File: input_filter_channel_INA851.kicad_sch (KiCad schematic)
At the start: 28 parts, among them K1 EE2-12TNU-L, U101 INA851

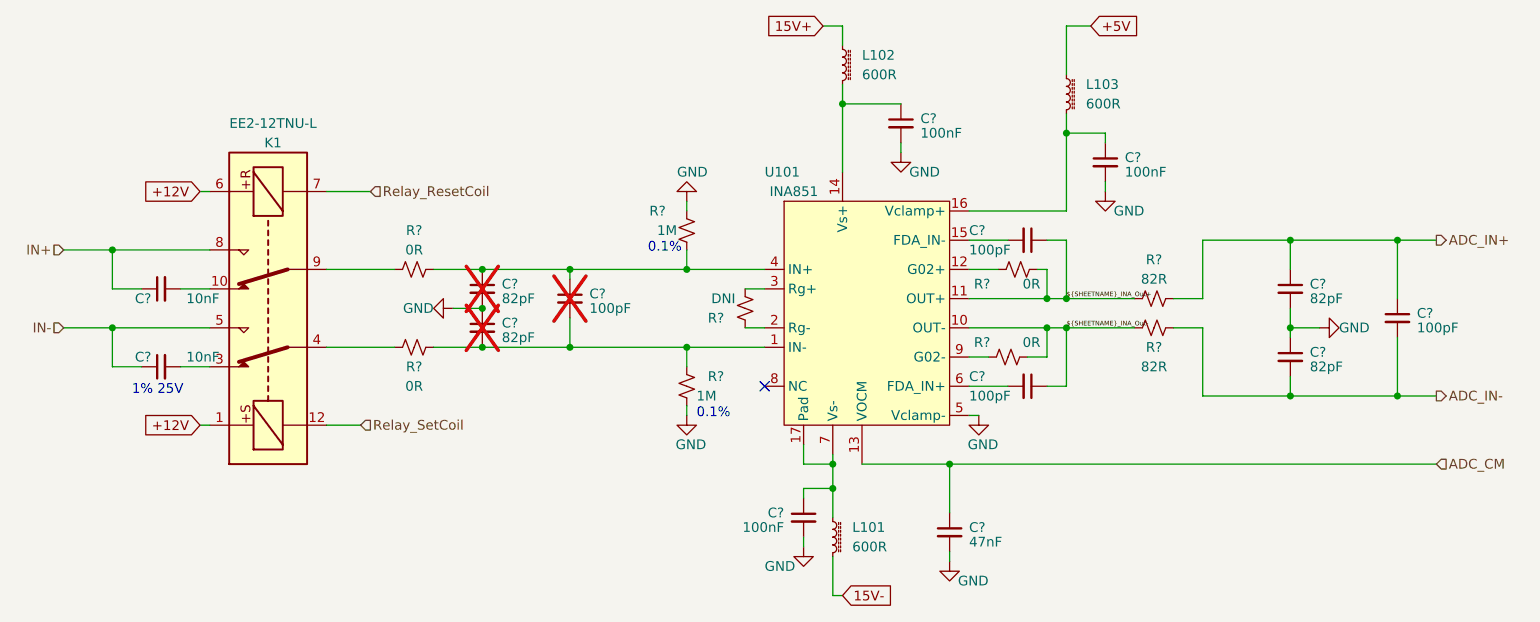
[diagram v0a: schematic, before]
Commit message: Updating design to cover reworks
Updating design to cover reworks.
This should now match what has been delivered to NASA GRE-ATF after the board reworks.
All outputs have been regenerated
Changes are:
1)Changed the clock splitter part to a 2.5V compatible part
2)Changed some caps on the MCLK lines to 0R resitors
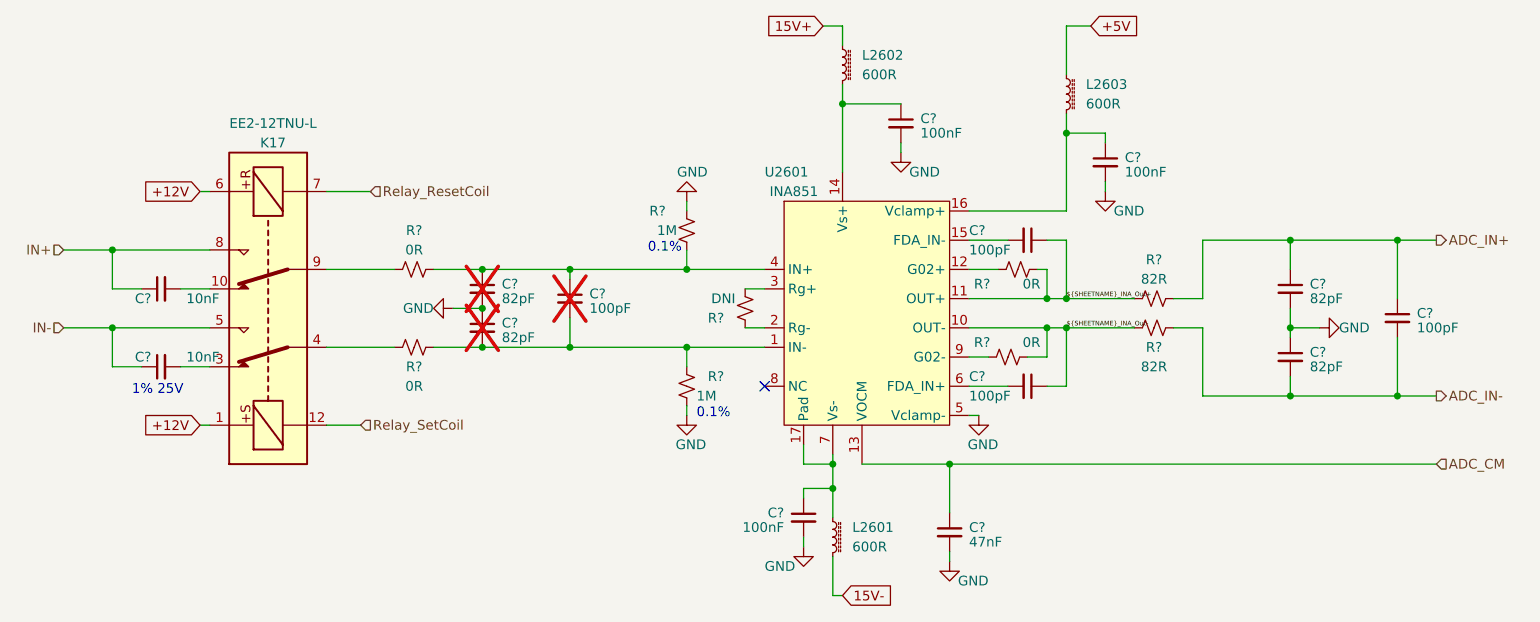
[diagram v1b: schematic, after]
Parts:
- R? (x4): footprint Resistor_SMD:R_0402_1005Metric -> Resistor_SMD:R_0603_1608Metric
- renumbered K1 to K17, L101 to L2601, L102 to L2602, L103 to L2603, U101 to U2601
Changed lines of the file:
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@@
 			)
 		)
-		(property "Footprint" "Resistor_SMD:R_0402_1005Metric"
+		(property "Footprint" "Resistor_SMD:R_0603_1608Metric"
 			(at 176.53 97.79 0)
 			(effects
@@
 			)
 		)
-		(property "Footprint" "Resistor_SMD:R_0402_1005Metric"
+		(property "Footprint" "Resistor_SMD:R_0603_1608Metric"
 			(at 177.8 86.36 0)
 			(effects
@@
 		(on_board yes)
 		(dnp no)
-		(property "Reference" "U101"
+		(property "Reference" "U2601"
 			(at 144.78 73.66 0)
 			(effects
@@
 		(dnp no)
 		(fields_autoplaced yes)
-		(property "Reference" "L101"
+		(property "Reference" "L2601"
 			(at 156.21 120.015 0)
 			(effects
@@
 		(dnp no)
 		(fields_autoplaced yes)
-		(property "Reference" "L103"
+		(property "Reference" "L2603"
 			(at 186.69 62.23 0)
 			(effects
@@
 			)
 		)
-		(property "Footprint" "Resistor_SMD:R_0402_1005Metric"
+		(property "Footprint" "Resistor_SMD:R_0603_1608Metric"
 			(at 99.06 86.36 0)
 			(effects
@@
 		(dnp no)
 		(fields_autoplaced yes)
-		(property "Reference" "L102"
+		(property "Reference" "L2602"
 			(at 157.48 58.42 0)
 			(effects
@@
 			)
 		)
-		(property "Footprint" "Resistor_SMD:R_0402_1005Metric"
+		(property "Footprint" "Resistor_SMD:R_0603_1608Metric"
 			(at 99.06 96.52 0)
 			(effects
@@
 		(on_board yes)
 		(dnp no)
-		(property "Reference" "K1"
+		(property "Reference" "K17"
 			(at 80.645 69.85 90)
 			(effects

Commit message: Opened & Saved Project in Kicad 9
- Opened & Saved Project in Kicad 9
- Added .gitignore from main
- Added sym-lib-table to link the unchanged symbol libs to the project
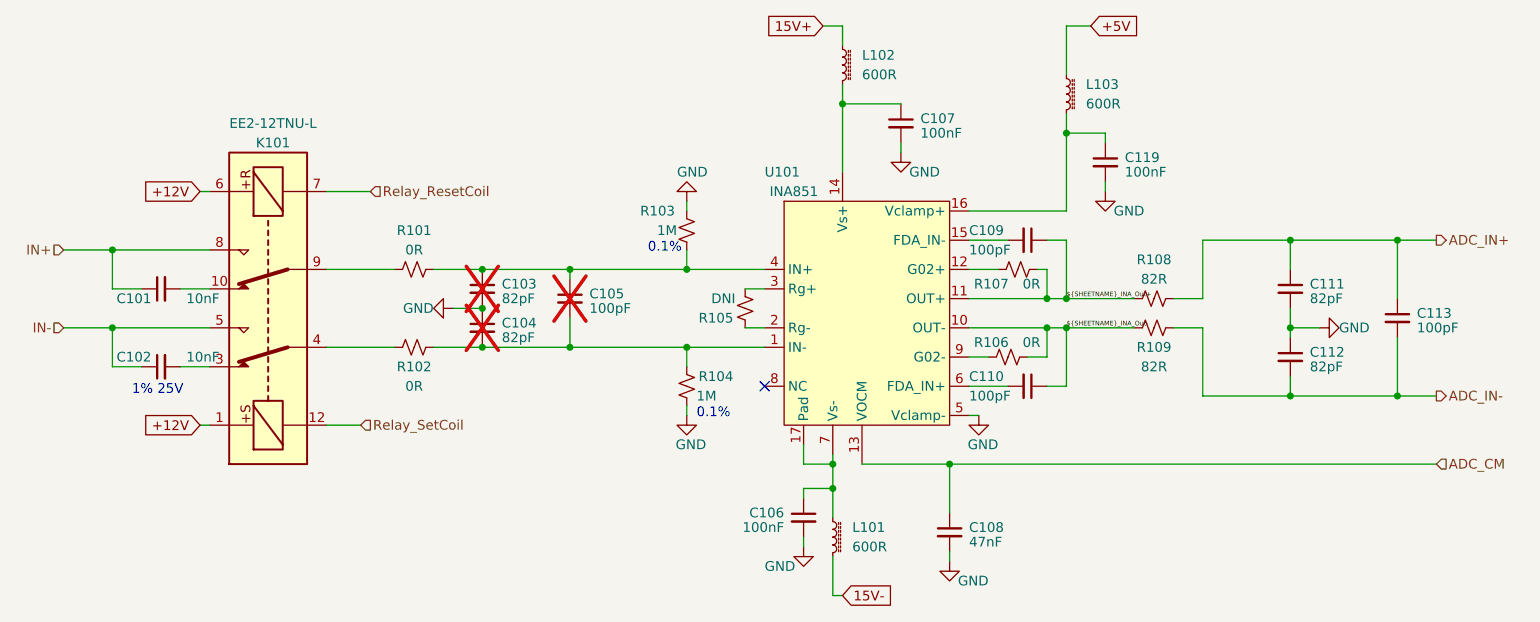
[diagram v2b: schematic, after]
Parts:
- gave numbers to parts that had none: 23
- renumbered K17 to K101, L2601 to L101, L2602 to L102, L2603 to L103, U2601 to U101
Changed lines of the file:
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@@
 (kicad_sch
-	(version 20231120)
+	(version 20250114)
 	(generator "eeschema")
-	(generator_version "8.0")
+	(generator_version "9.0")
 	(paper "A4")
 	(title_block
@@
 		(company "OspreyDCS")
 	)
+	(text "1% 25V\n"
+		(exclude_from_sim no)
+		(at 62.23 102.87 0)
+		(effects
+			(font
+				(size 1.27 1.27)
+			)
+			(justify left bottom)
+		)
+	)
+	(text "0.1%\n\n"
+		(exclude_from_sim no)
+		(at 129.54 86.36 0)
+		(effects
+			(font
+				(size 1.27 1.27)
+			)
+			(justify left bottom)
+		)
+	)
+	(text "0.1%\n\n"
+		(exclude_from_sim no)
+		(at 135.89 107.95 0)
+		(effects
+			(font
+				(size 1.27 1.27)
+			)
+			(justify left bottom)
+		)
+	)
 	(junction
 		(at 59.69 93.98)
@@
 		)
 	)
-	(text "1% 25V\n"
-		(exclude_from_sim no)
-		(at 62.23 102.87 0)
-		(effects
-			(font
-				(size 1.27 1.27)
-			)
-			(justify left bottom)
-		)
-	)
-	(text "0.1%\n\n"
-		(exclude_from_sim no)
-		(at 129.54 86.36 0)
-		(effects
-			(font
-				(size 1.27 1.27)
-			)
-			(justify left bottom)
-		)
-	)
-	(text "0.1%\n\n"
-		(exclude_from_sim no)
-		(at 135.89 107.95 0)
-		(effects
-			(font
-				(size 1.27 1.27)
-			)
-			(justify left bottom)
-		)
-	)
 	(label "${SHEETNAME}_INA_Out-"
 		(at 184.15 93.98 0)
-		(fields_autoplaced yes)
 		(effects
 			(font
@@
 	(label "${SHEETNAME}_INA_Out+"
 		(at 184.15 90.17 0)
-		(fields_autoplaced yes)
 		(effects
 			(font
@@
 		(shape input)
 		(at 93.345 76.2 0)
-		(fields_autoplaced yes)
 		(effects
 			(font
@@
 		(shape input)
 		(at 92.075 106.68 0)
-		(fields_autoplaced yes)
 		(effects
 			(font
@@
 		(shape input)
 		(at 53.34 93.98 180)
-		(fields_autoplaced yes)
 		(effects
 			(font
@@
 		(shape output)
 		(at 232.41 102.87 0)
-		(fields_autoplaced yes)
 		(effects
 			(font
@@
 		(shape input)
 		(at 232.41 111.76 0)
-		(fields_autoplaced yes)
 		(effects
 			(font
@@
 		(shape input)
 		(at 53.34 83.82 180)
-		(fields_autoplaced yes)
 		(effects
 			(font
@@
 		(shape output)
 		(at 232.41 82.55 0)
-		(fields_autoplaced yes)
 		(effects
 			(font
@@
 		(on_board yes)
 		(dnp no)
-		(property "Reference" "C?"
+		(property "Reference" "C102"
 			(at 64.77 97.79 90)
 			(effects
@@
 		(on_board yes)
 		(dnp no)
-		(property "Reference" "#PWR?"
+		(property "Reference" "#PWR0107"
 			(at 162.56 77.47 0)
 			(effects
@@
 		(on_board yes)
 		(dnp no)
-		(property "Reference" "#PWR?"
+		(property "Reference" "#PWR0108"
 			(at 168.91 130.81 0)
 			(effects
@@
 		(on_board yes)
 		(dnp yes)
-		(property "Reference" "C?"
+		(property "Reference" "C105"
 			(at 121.92 89.5413 0)
 			(effects
@@
 		(on_board yes)
 		(dnp no)
-		(property "Reference" "R?"
+		(property "Reference" "R103"
 			(at 130.81 78.74 0)
 			(effects
@@
 		(on_board yes)
 		(dnp no)
-		(property "Reference" "C?"
+		(property "Reference" "C112"
 			(at 215.9 97.1613 0)
 			(effects
@@
 		(on_board yes)
 		(dnp no)
-		(property "Reference" "#PWR?"
+		(property "Reference" "#PWR0106"
 			(at 149.86 128.905 0)
 			(effects
@@
 		(on_board yes)
 		(dnp no)
-		(property "Reference" "R?"
+		(property "Reference" "R105"
 			(at 138.43 92.71 0)
 			(effects
@@
 		(on_board yes)
 		(dnp no)
-		(property "Reference" "R?"
+		(property "Reference" "R106"
 			(at 172.085 95.885 90)
 			(effects
@@
 		(on_board yes)
 		(dnp no)
-		(property "Reference" "C?"
+		(property "Reference" "C113"
 			(at 229.87 92.0813 0)
 			(effects
@@
 		(on_board yes)
 		(dnp no)
-		(property "Reference" "R?"
+		(property "Reference" "R107"
 			(at 172.085 88.265 90)
 			(effects
@@
 		(on_board yes)
 		(dnp no)
-		(property "Reference" "C?"
+		(property "Reference" "C110"
 			(at 171.45 100.33 90)
 			(effects
@@
 		(on_board yes)
 		(dnp no)
-		(property "Reference" "#PWR?"
+		(property "Reference" "#PWR0132"
 			(at 189.23 82.55 0)
 			(effects
@@
 		(on_board yes)
 		(dnp no)
-		(property "Reference" "#PWR?"
+		(property "Reference" "#PWR0111"
 			(at 223.52 93.98 0)
 			(effects
@@
 		(on_board yes)
 		(dnp no)
-		(property "Reference" "U2601"
+		(property "Reference" "U101"
 			(at 144.78 73.66 0)
 			(effects
@@
 		(on_board yes)
 		(dnp no)
-		(property "Reference" "#PWR?"
+		(property "Reference" "#PWR0109"
 			(at 172.72 111.76 0)
 			(effects
@@
 		(on_board yes)
 		(dnp no)
-		(property "Reference" "C?"
+		(property "Reference" "C119"
 			(at 191.77 71.7613 0)
 			(effects
@@
 		(dnp no)
 		(fields_autoplaced yes)
-		(property "Reference" "L2601"
+		(property "Reference" "L101"
 			(at 156.21 120.015 0)
 			(effects
@@
 		(on_board yes)
 		(dnp no)
-		(property "Reference" "C?"
+		(property "Reference" "C111"
 			(at 215.9 88.2713 0)
 			(effects
@@
 		(on_board yes)
 		(dnp no)
-		(property "Reference" "C?"
+		(property "Reference" "C109"
 			(at 171.45 81.28 90)
 			(effects
@@
 		(on_board yes)
 		(dnp no)
-		(property "Reference" "C?"
+		(property "Reference" "C107"
 			(at 165.1 66.6813 0)
 			(effects
@@
 		(on_board yes)
 		(dnp no)
-		(property "Reference" "C?"
+		(property "Reference" "C108"
 			(at 171.45 120.0213 0)
 			(effects
@@
 		(on_board yes)
 		(dnp yes)
-		(property "Reference" "C?"
+		(property "Reference" "C104"
 			(at 110.49 93.3513 0)
 			(effects
@@
 		(dnp no)
 		(fields_autoplaced yes)
-		(property "Reference" "L2603"
+		(property "Reference" "L103"
 			(at 186.69 62.23 0)
 			(effects
@@
 		(dnp no)
 		(fields_autoplaced yes)
-		(property "Reference" "R?"
+		(property "Reference" "R101"
 			(at 99.06 81.28 90)
 			(effects
@@
 		(on_board yes)
 		(dnp no)
-		(property "Reference" "#PWR?"
+		(property "Reference" "#PWR0103"
 			(at 97.79 91.44 0)
 			(effects
@@
 		(dnp no)
 		(fields_autoplaced yes)
-		(property "Reference" "L2602"
+		(property "Reference" "L102"
 			(at 157.48 58.42 0)
 			(effects
@@
 		(on_board yes)
 		(dnp no)
-		(property "Reference" "C?"
+		(property "Reference" "C106"
 			(at 147.32 118.1163 0)
 			(effects
@@
 		(on_board yes)
 		(dnp no)
-		(property "Reference" "#PWR?"
+		(property "Reference" "#PWR0104"
 			(at 134.62 71.12 0)
 			(effects
@@
 		(on_board yes)
 		(dnp no)
-		(property "Reference" "#PWR?"
+		(property "Reference" "#PWR0105"
 			(at 134.62 111.76 0)
 			(effects
@@
 		(on_board yes)
 		(dnp yes)
-		(property "Reference" "C?"
+		(property "Reference" "C103"
 			(at 110.49 88.2713 0)
 			(effects
@@
 		(dnp no)
 		(fields_autoplaced yes)
-		(property "Reference" "R?"
+		(property "Reference" "R108"
 			(at 195.58 85.09 90)
 			(effects
@@
 		(on_board yes)
 		(dnp no)
-		(property "Reference" "R?"
+		(property "Reference" "R104"
 			(at 138.43 100.33 0)
 			(effects
@@
 		(on_board yes)
 		(dnp no)
-		(property "Reference" "R?"
+		(property "Reference" "R109"
 			(at 195.58 96.52 90)
 			(effects
@@
 		(on_board yes)
 		(dnp no)
-		(property "Reference" "R?"
+		(property "Reference" "R102"
 			(at 99.06 99.06 90)
 			(effects
@@
 		(on_board yes)
 		(dnp no)
-		(property "Reference" "K17"
+		(property "Reference" "K101"
 			(at 80.645 69.85 90)
 			(effects
@@
 		(on_board yes)
 		(dnp no)
-		(property "Reference" "C?"
+		(property "Reference" "C101"
 			(at 64.77 90.17 90)
 			(effects

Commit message: Fixed Serveral ERC errors
Fixed Several ERC errors
- Ignored off-grid connections errors

- Updated a number of symbols from the Kicad default library. This should have no visual change
  - Power:Ground
  - Power:Earth
  - Device:LED

- Relinked some symbols with a new copy in the AD7688_Digitaizer_SLib. This was to fix errors/warnings where local schematic changes were made. This process was opening the local symbol; saving a copy in the AD7688_Digitaizer_SLib; relinking the part to the new part in the AD7688_Digitaizer_SLib. This should have caused no visual change.
  - EC2-12TNU relays parts (K101 etc.)
  - U36 TL071
  - U16 SI5330 (had local edit to add pin25-gnd pad)
  - U32 TXU101

- Changed D4 symbol to explicitly show the unused pin on the schematic (was an error)

- Removed an extra pin 25 from U35 showing the pad connection. Renamed the pin for clarity
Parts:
- K101: symbol Relay:EC2-12TNU -> AD7768_Digitizer_SLib:EC2-12TNU
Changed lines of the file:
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@@
 	)
 	(symbol
-		(lib_id "Relay:EC2-12TNU")
+		(lib_id "AD7768_Digitizer_SLib:EC2-12TNU")
 		(at 80.01 91.44 90)
 		(unit 1)

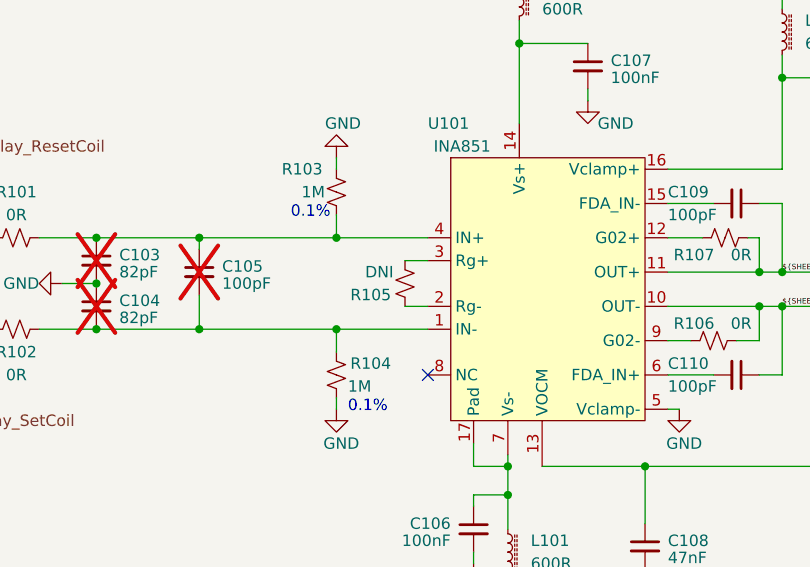
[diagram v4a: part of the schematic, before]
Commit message: Verified 'Must do changes' implemented all 'should do' changes
Must do Changes that have been verified:
-Change the Clock divider chip to the 2,5V part
-Remove AC coupling caps in clock lines

Should do changes implmented
  - Add pull up resistor to ADC reset lines
  - Internal termination of PPS (when unused)
  - Add Heat Sinking to inductors by increased traces/planes size (Copied/Based-On from V2 Design)
  - Changed to a 2.048V VREF with accompanying removal of INA851 gain resistor (this will give more dynamic range)
  - Move ground test points further away from power rails

Also Included Some Improvments to the power rails seen in V2 when in comes to:
-12V rail into the power section and up to the front of the board
-The 3.3V rail that goes around the edge of the board to the relay switch IC's

Note - DRC warnings that exist are either ignorable, or pointing to the fact that the default footprint libs may have been changed in Kicad9 causeing a mismatch to what is on the board. I will no update these footprint to the new version yet, or possibly ever.
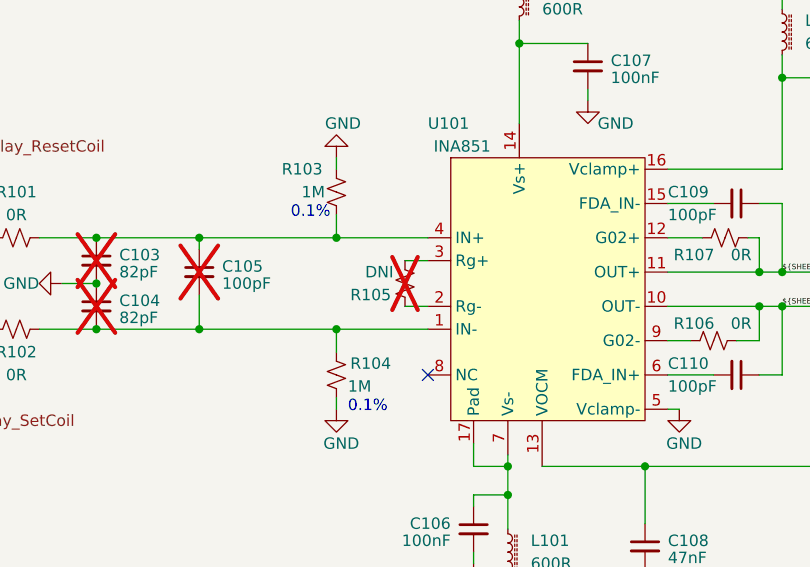
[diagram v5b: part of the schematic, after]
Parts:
- R105: now not fitted
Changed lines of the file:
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@@
 		(in_bom yes)
 		(on_board yes)
-		(dnp no)
+		(dnp yes)
 		(property "Reference" "R105"
 			(at 138.43 92.71 0)
